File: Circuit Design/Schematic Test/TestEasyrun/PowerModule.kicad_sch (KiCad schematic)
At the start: 33 parts

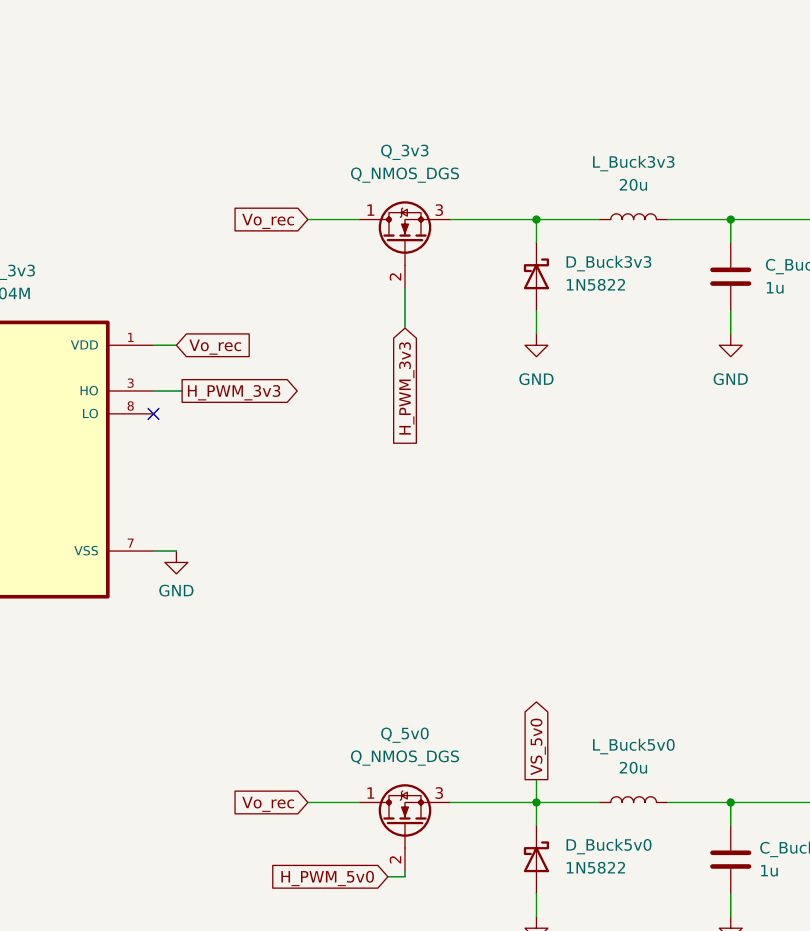
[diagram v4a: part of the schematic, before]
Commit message: Almost all footprints added
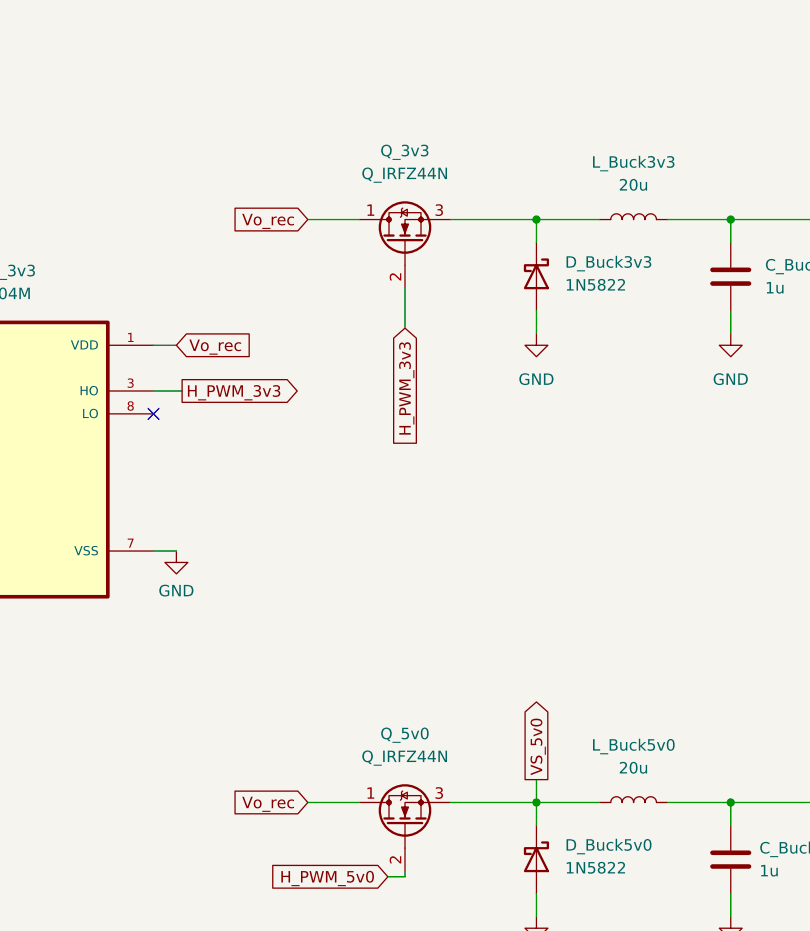
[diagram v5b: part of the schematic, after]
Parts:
- L_Buck3v3, L_Buck5v0: footprint (none) -> Inductor_THT:L_Toroid_Vertical_L25.4mm_W14.7mm_P12.20mm_Vishay_TJ5_BigPads
- Q_3v3, Q_5v0: value Q_NMOS_DGS -> Q_IRFZ44N; footprint (none) -> Package_TO_SOT_THT:TO-220-3_Vertical
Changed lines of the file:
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@@
     (in_bom yes) (on_board yes) (fields_autoplaced)
     (property "Reference" "Q_5v0" (id 0) (at 217.805 106.68 90))
-    (property "Value" "Q_NMOS_DGS" (id 1) (at 217.805 109.22 90))
-    (property "Footprint" "" (id 2) (at 215.265 111.76 0)
+    (property "Value" "Q_IRFZ44N" (id 1) (at 217.805 109.22 90))
+    (property "Footprint" "Package_TO_SOT_THT:TO-220-3_Vertical" (id 2) (at 215.265 111.76 0)
       (effects (font (size 1.27 1.27)) hide)
     )
@@
     (property "Reference" "L_Buck3v3" (id 0) (at 243.205 43.18 90))
     (property "Value" "20u" (id 1) (at 243.205 45.72 90))
-    (property "Footprint" "" (id 2) (at 243.205 49.53 0)
+    (property "Footprint" "Inductor_THT:L_Toroid_Vertical_L25.4mm_W14.7mm_P12.20mm_Vishay_TJ5_BigPads" (id 2) (at 243.205 49.53 0)
       (effects (font (size 1.27 1.27)) hide)
     )
@@
     (property "Reference" "L_Buck5v0" (id 0) (at 243.205 107.95 90))
     (property "Value" "20u" (id 1) (at 243.205 110.49 90))
-    (property "Footprint" "" (id 2) (at 243.205 114.3 0)
+    (property "Footprint" "Inductor_THT:L_Toroid_Vertical_L25.4mm_W14.7mm_P12.20mm_Vishay_TJ5_BigPads" (id 2) (at 243.205 114.3 0)
       (effects (font (size 1.27 1.27)) hide)
     )
@@
     (in_bom yes) (on_board yes) (fields_autoplaced)
     (property "Reference" "Q_3v3" (id 0) (at 217.805 41.91 90))
-    (property "Value" "Q_NMOS_DGS" (id 1) (at 217.805 44.45 90))
-    (property "Footprint" "" (id 2) (at 215.265 46.99 0)
-      (effects (font (size 1.27 1.27)) hide)
-    )
+    (property "Value" "Q_IRFZ44N" (id 1) (at 217.805 44.45 90))
+    (property "Footprint" "Package_TO_SOT_THT:TO-220-3_Vertical" (id 2) (at 215.265 46.99 0)
+      (effects (font (size 1.27 1.27)) hide)
+    )

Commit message: PWM generator file
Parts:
- removed CBT_3v3, CBT_5v0: C, Capacitor_SMD:C_0805_2012Metric_Pad1.18x1.45mm_HandSolder, symbol Device:C
- removed C_CT_PWM_3v3, C_CT_PWM_5v0: 1n, Capacitor_SMD:C_0805_2012Metric_Pad1.18x1.45mm_HandSolder, symbol Device:C
- removed C_DTCS_3v3, C_DTCS_5v0: 1u, Capacitor_SMD:C_0805_2012Metric_Pad1.18x1.45mm_HandSolder, symbol Device:C
- removed DBT_3v3, DBT_5v0: D, Diode_THT:D_DO-201AD_P15.24mm_Horizontal, symbol Device:D
- removed Driver_3v3, Driver_5v0: LM5104M, LM5104M:SOIC127P599X175-8N, symbol LM5104M:LM5104M
- removed RT_3v3, RT_5v0: R, Resistor_SMD:R_0805_2012Metric_Pad1.20x1.40mm_HandSolder, symbol Device:R
- removed R_DTCS_3v3, R_DTCS_5v0: 680, Resistor_SMD:R_0805_2012Metric_Pad1.20x1.40mm_HandSolder, symbol Device:R
- removed R_DTC_3v3, R_DTC_5v0: 1k, Resistor_SMD:R_0805_2012Metric_Pad1.20x1.40mm_HandSolder, symbol Device:R
- removed R_RT_PWM_3v3, R_RT_PWM_5v0: 6.8k, Resistor_SMD:R_0805_2012Metric_Pad1.20x1.40mm_HandSolder, symbol Device:R
- removed Rdiv1_3v3: 100k, Resistor_SMD:R_0805_2012Metric_Pad1.20x1.40mm_HandSolder, symbol Device:R
- removed Rdiv2_3v3: 51k, Resistor_SMD:R_0805_2012Metric_Pad1.20x1.40mm_HandSolder, symbol Device:R
- removed U_PWM_3v3, U_PWM_5v0: TL494CDR, TL494CDR_PWM:SOIC127P600X175-16N, symbol TL494CDR:TL494CDR
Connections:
- net H_PWM_3v3 is gone; now on net PWM_3v3: Q_3v3.2 (G)
- net H_PWM_5v0 is gone; now on net PWM_5v0: Q_5v0.2 (G)
- net 3v3 renamed 3v3_out
- net 5v0 renamed 5v0_out
- no-connect marks 4 -> 0
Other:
- added sheet PWM_Generator_3v3 (PWM_Generator_3v3.kicad_sch)
- added sheet PWM_Generator_5v0 (PWM_Generator_5v0.kicad_sch)
- moved on the sheet: C_Buck3v3, C_Buck5v0, C_rec, D_Buck3v3, D_Buck5v0, D_S1, D_S2, L_Buck3v3, L_Buck5v0, Q_3v3, Q_5v0

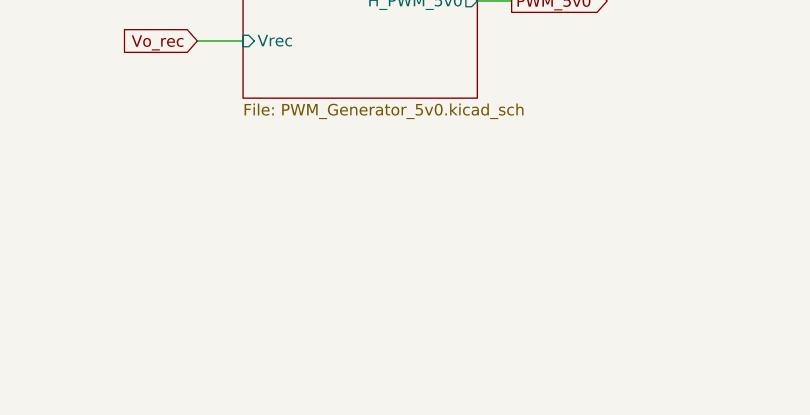
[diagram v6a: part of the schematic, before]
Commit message: Include the battery power module
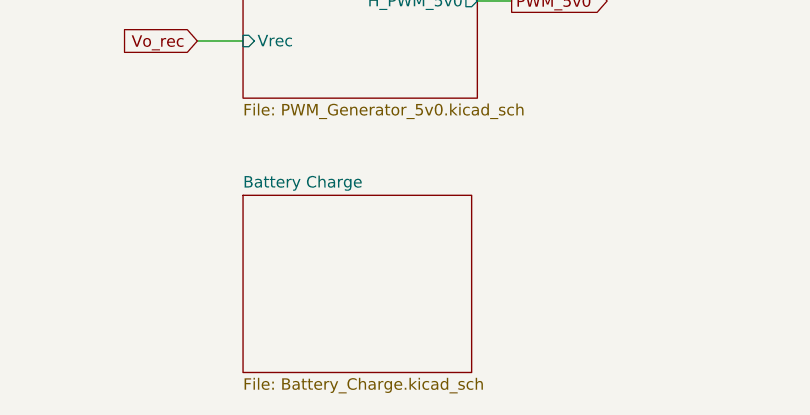
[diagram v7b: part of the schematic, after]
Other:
- added sheet Battery Charge (Battery_Charge.kicad_sch)
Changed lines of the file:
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@@
+    )
+  )
+  (sheet (at 125.73 131.445) (size 25.4 19.685) (fields_autoplaced)
+    (stroke (width 0.1524) (type solid) (color 0 0 0 0))
+    (fill (color 0 0 0 0.0000))
+    (property "Sheet name" "Battery Charge" (id 0) (at 125.73 130.7334 0)
+      (effects (font (size 1.27 1.27)) (justify left bottom))
+    )
+    (property "Sheet file" "Battery_Charge.kicad_sch" (id 1) (at 125.73 151.7146 0)
+      (effects (font (size 1.27 1.27)) (justify left top))
     )
   )

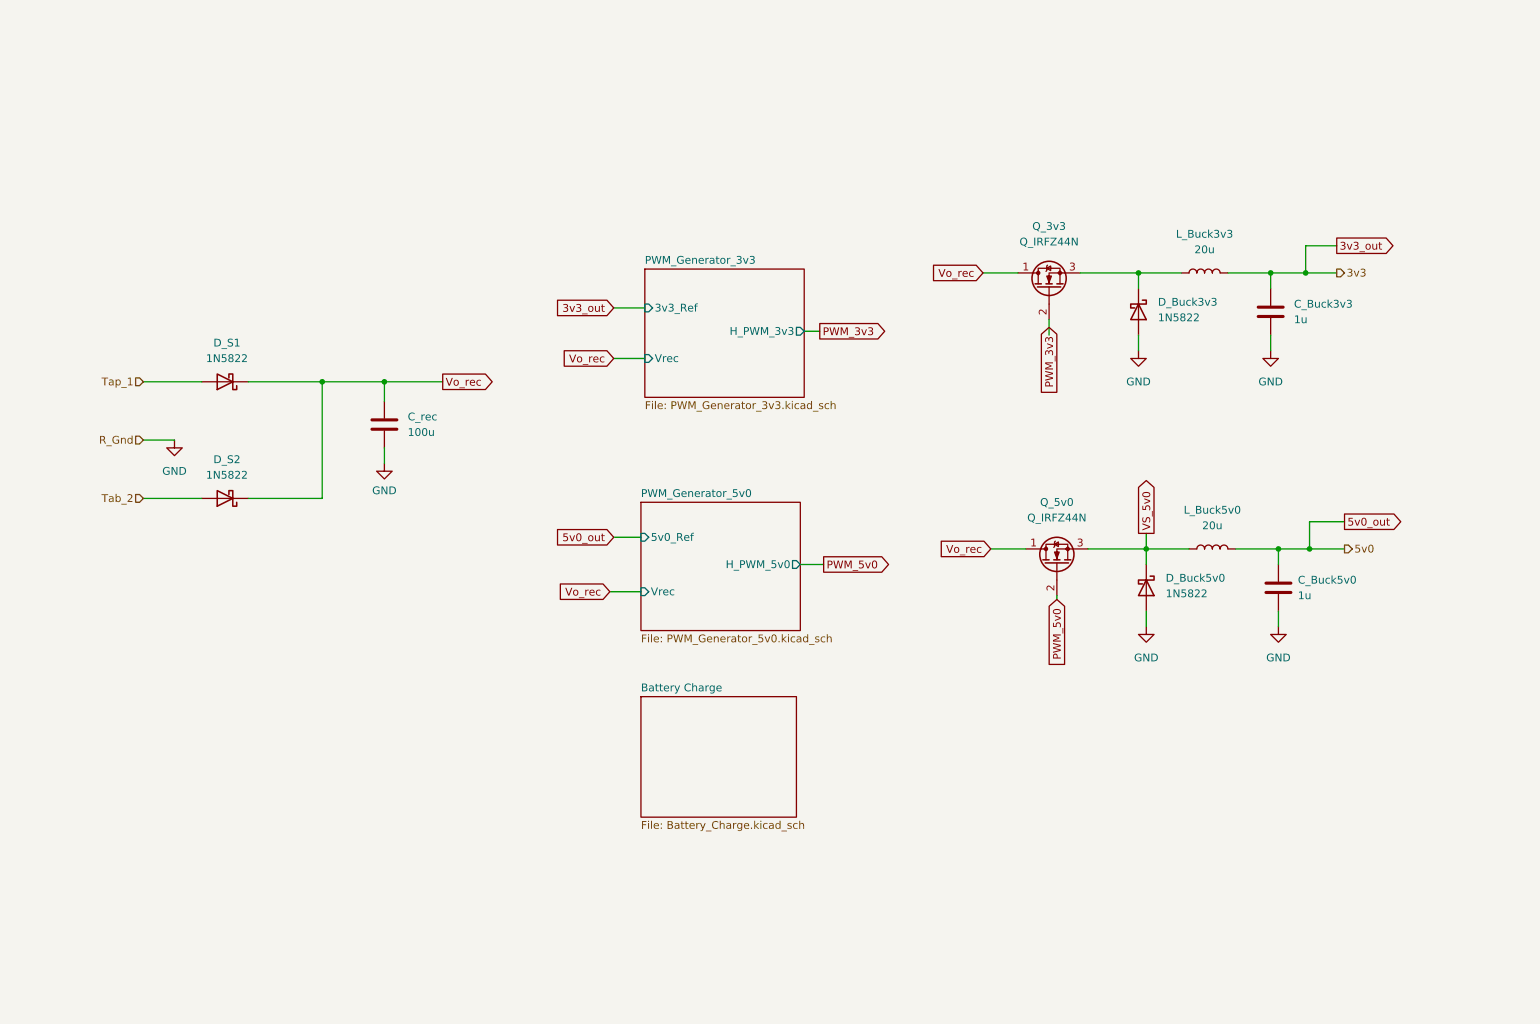
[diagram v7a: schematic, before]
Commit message: Change the global labels
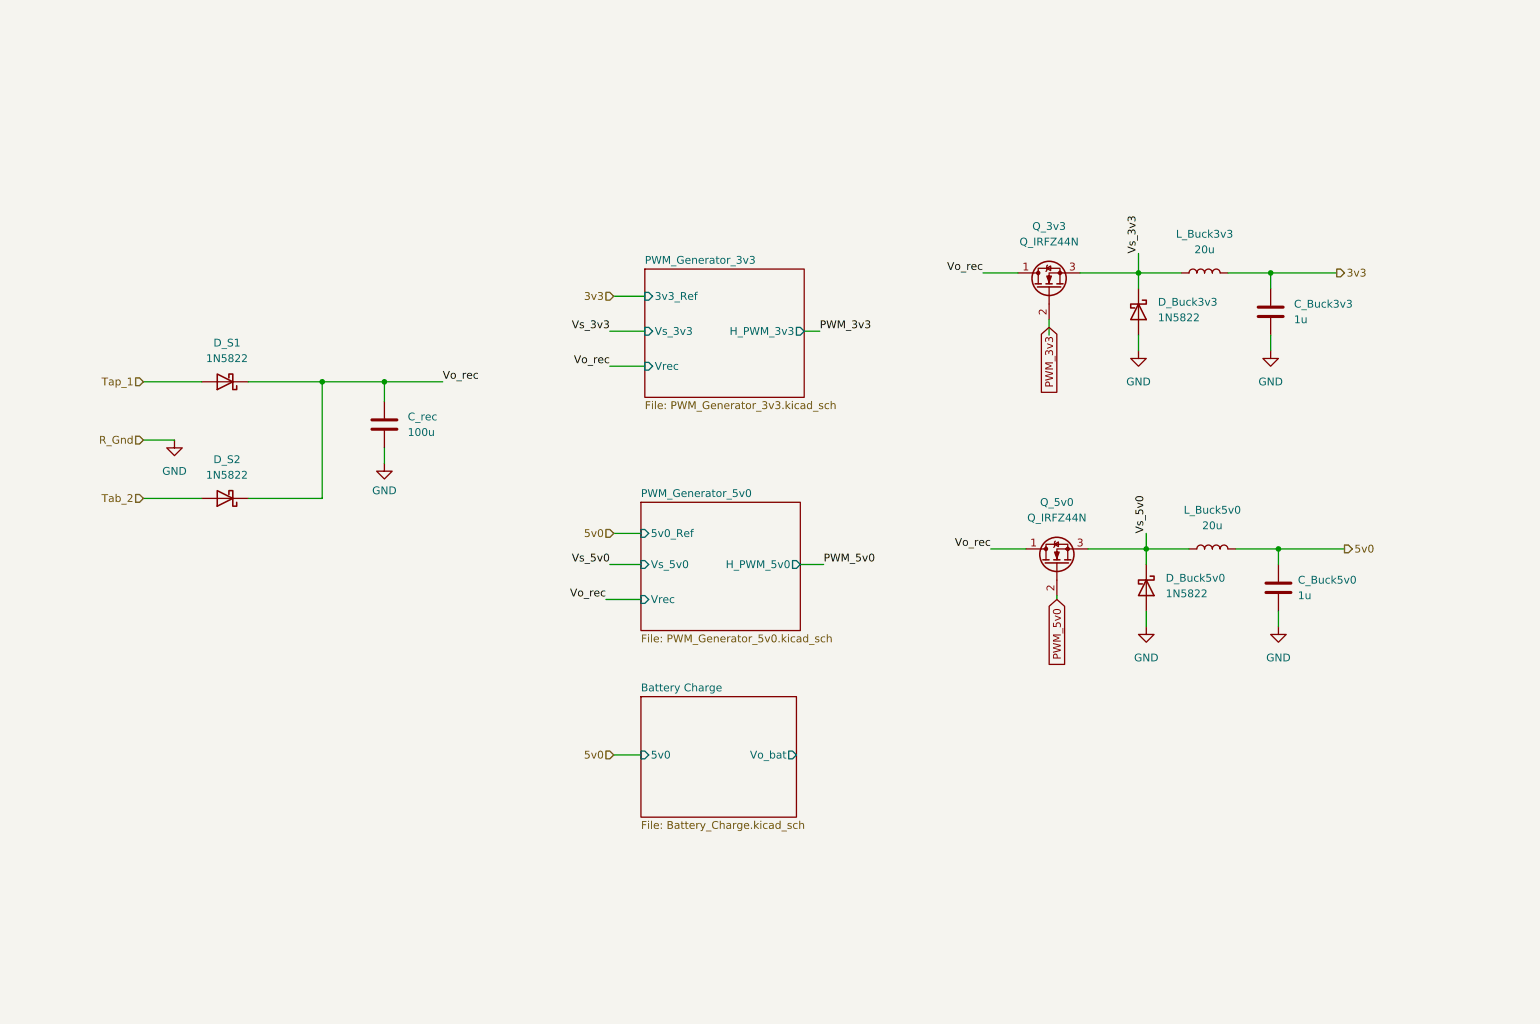
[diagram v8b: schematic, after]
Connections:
- net Vs_3v3: now reaches D_Buck3v3.1 (K), L_Buck3v3.1, Q_3v3.3 (S)
- net 3v3_out renamed 3v3
- net 5v0_out renamed 5v0
- net VS_5v0 renamed Vs_5v0
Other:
- sheet Battery Charge ports: added 5v0, Vo_bat; removed none
- sheet PWM_Generator_3v3 ports: added Vs_3v3; removed none
- sheet PWM_Generator_5v0 ports: added Vs_5v0; removed none
